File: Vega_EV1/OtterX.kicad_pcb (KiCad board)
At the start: 4 copper layers, 170.1 x 170.1 mm, 180 parts, among them J1 VERA_CONN, J10 1.5MB RAM Expansion, J11 KMDGX-6SG, J12 VIA1 Extra Pins, J14 Flash WR EN, J16 ATX-24, J17 SNES23, J18 SNES0, J19 SNES1, J2 VIA2 Header, J21 ISP, J25 PS2 Pwr Src, J26 Front Panel, J27 EXTRAM_ENABLE, J29 AudioPlug3, J3 IEC, J5 YM CT Out, J6 Ext. NMI, J7 RTC GPIO, J9 I2C, K1 HK19F, P1 60 Pin Edge Conn, Q1 2N7000, Q2 2N7000, Q3 2N7000, SW1 FSM4JH, SW2 FSM4JH, SW3 FSM4JH, U1 W65C02S, U11 74ACT163, U12 ATtiny861-20P, U13 MCP7940N-xP, U14 74AHCT00, U15 74AHCT02, U16 74AHCT04, U17 74AHCT02, U18 74AHCT32, U19 74AHCT20, U2 W65C22S, U20 74AHCT20, U21 74AHCT138, U22 TL074, U24 YM2151, U25 YM3012, U26 LM324, U4 74AHCT10, U5 74AHCT273, U6 74AHCT273, U7 SST39SF040, U8 AS6C1008-55PCN, U9 AS6C4008-55PCN, X1 ACH-16.000MHZ-EK, X2 ECS-2100AX-3.579545MHZ, Y1 ECS-.327-6-13X

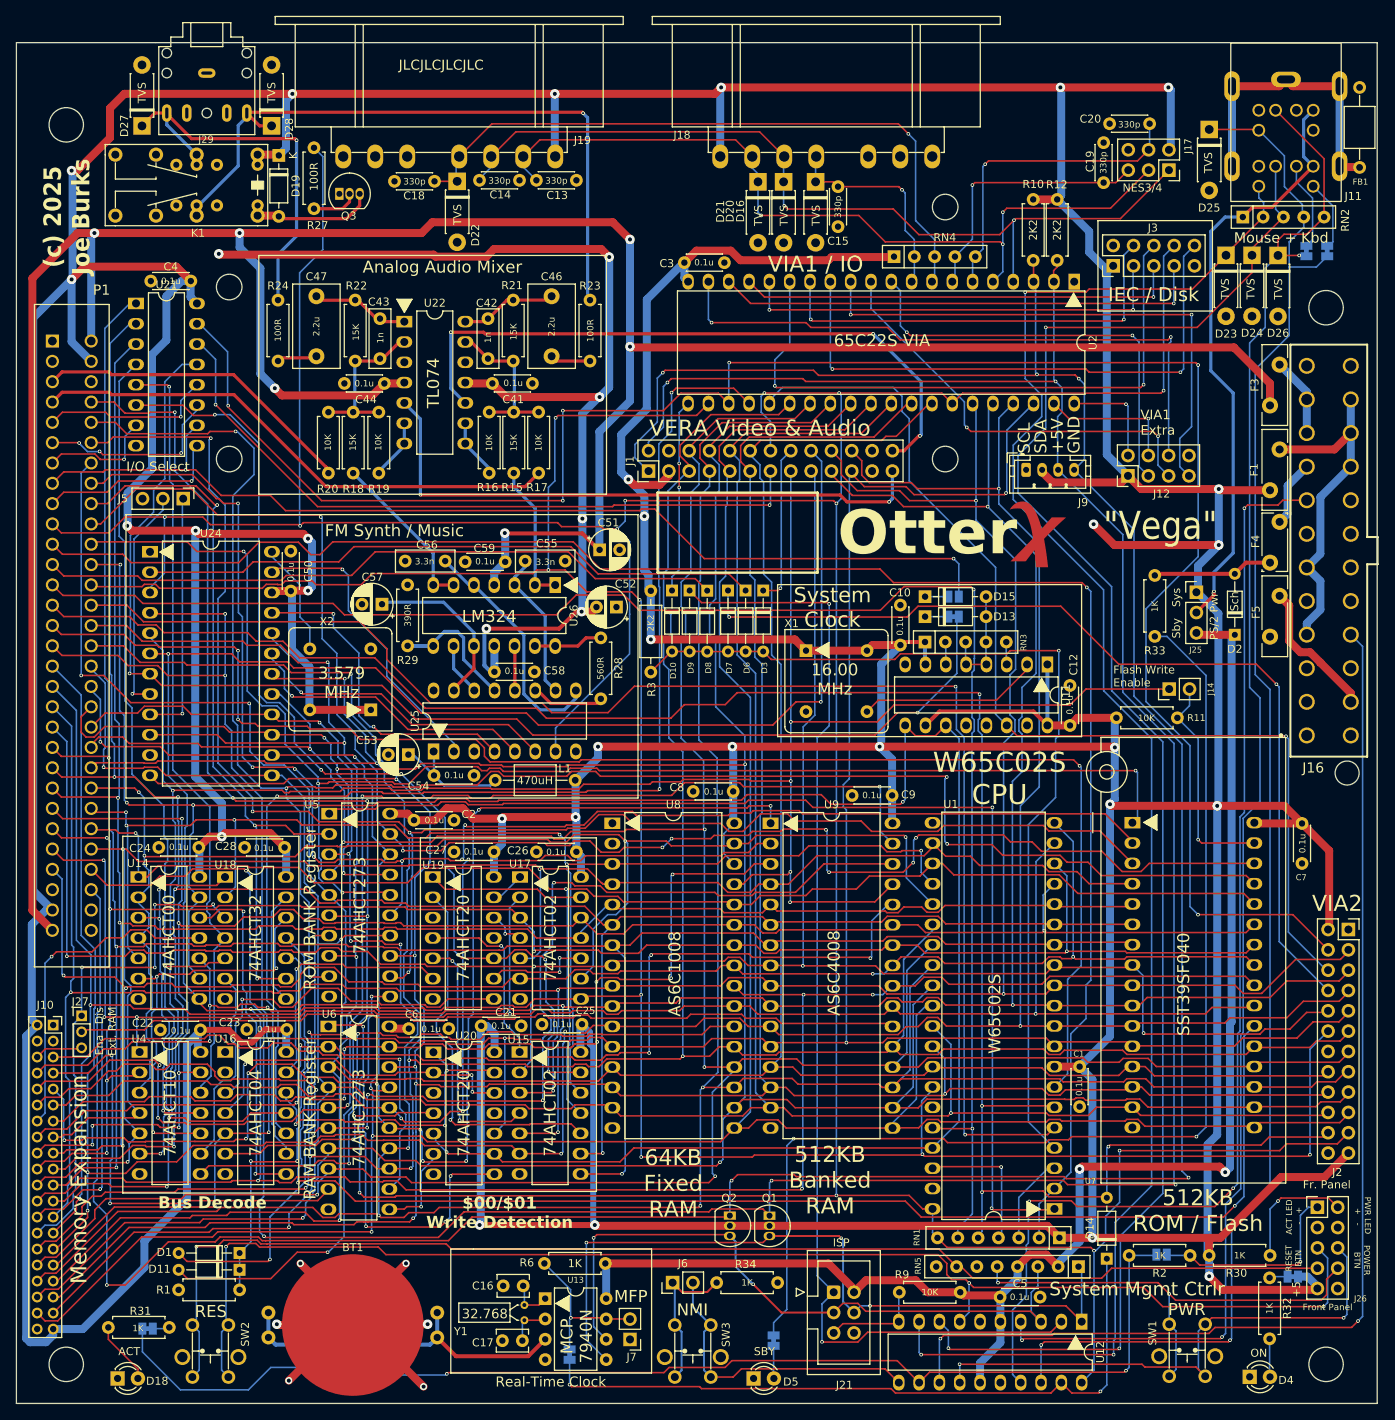
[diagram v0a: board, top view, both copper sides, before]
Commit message: Fix #16, widen transistor footprints
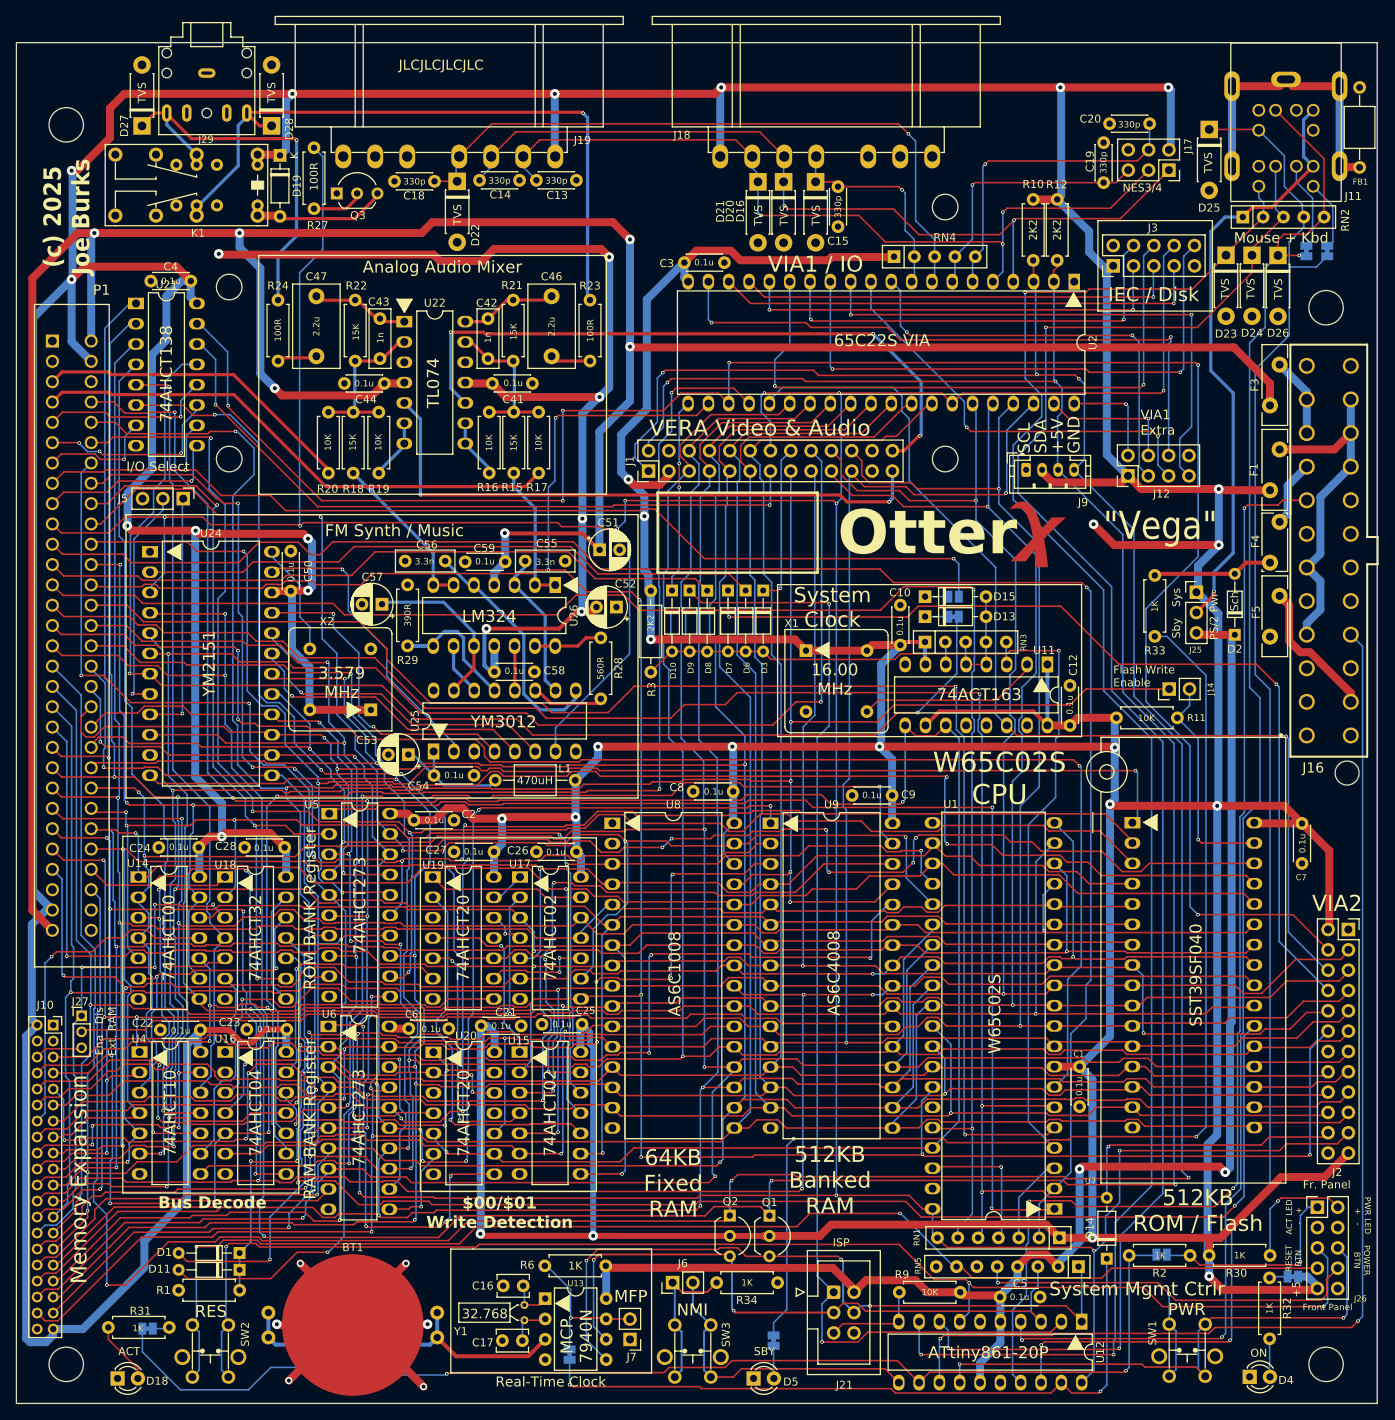
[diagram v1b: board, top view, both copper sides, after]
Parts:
- Q1, Q2, Q3: footprint Package_TO_SOT_THT:TO-92_Inline -> Package_TO_SOT_THT:TO-92_Inline_Wide
- moved Q3 0.32 mm to (63.0, 31.1)
- moved R6 0.30 mm to (89.0, 165.1)
- moved D19 0.15 mm to (55.9, 26.3)
- moved R1 0.05 mm to (50.8, 168.2)
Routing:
- net /SMC/SMC_SDA: track 94.0 -> 89.9 mm
- net +5V: track 1487.2 -> 1490.8 mm
- net /SMC/RESBTN_PD: track 159.6 -> 162.7 mm, vias 1 -> 2
- net Net-(D19-A): track 14.5 -> 16.1 mm
- net /SMC/SMC_SCL: track 84.2 -> 82.7 mm
- net Net-(Q3-G): track 5.79 -> 6.51 mm
- net ~{ROMEN}: track 175.5 -> 176.2 mm
- net /SMC/RES_BTN: track 172.0 -> 171.4 mm
